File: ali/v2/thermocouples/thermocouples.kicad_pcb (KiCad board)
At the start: 4 copper layers, 85 x 76 mm, 169 parts, among them J1 Conn_02x01, J10 Conn_01x02, J11 Conn_01x02, J12 Conn_01x02, J13 Conn_01x02, J14 Conn_01x02, J15 Conn_01x15, J2 Conn_01x05, J3 USB_C_Receptacle_USB2.0_16P, J5 Conn_02x09_Counter_Clockwise, J6 Screw_Terminal_01x02, J7 Conn_01x03, J8 Vertical Ethernet, J9 Conn_01x02, SW1 SKRPANE010, U1 STM32H563RIV6, U10 TMP117AIDRVR, U11 TMP117AIDRVR, U12 TMP117AIDRVR, U13 TMP117AIDRVR, U2 UCC33420-Q1, U3 AP2112K-3.3, U4 TJA1462ATK, U5 LAN8742AI, U6 ADS124S08, U7 TCA9543A, U8 TMP117AIDRVR, U9 TMP117AIDRVR, Y1 25 MHz, Y2 25 MHz

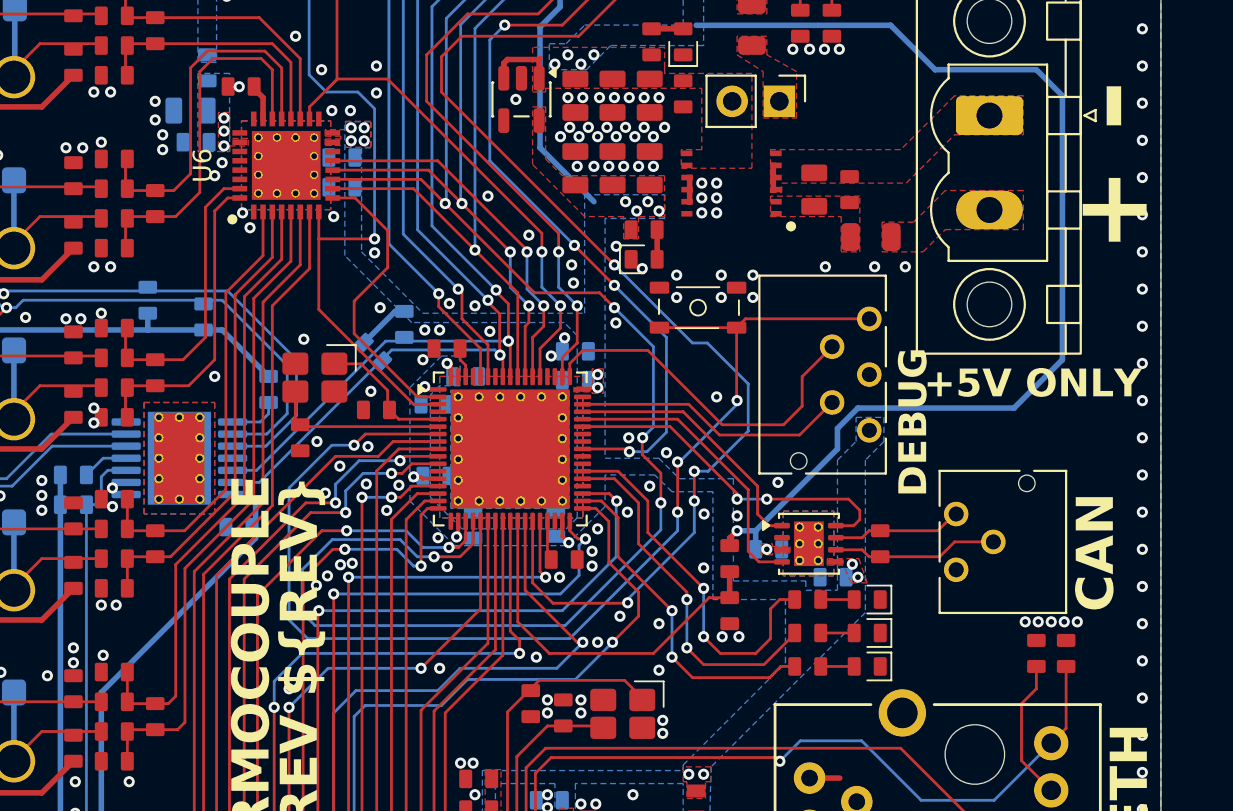
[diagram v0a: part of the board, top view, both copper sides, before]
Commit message: Globally remove LCSC labels, update MPNs and IOCs, add +5V monitoring to DAQs, fix some footprints
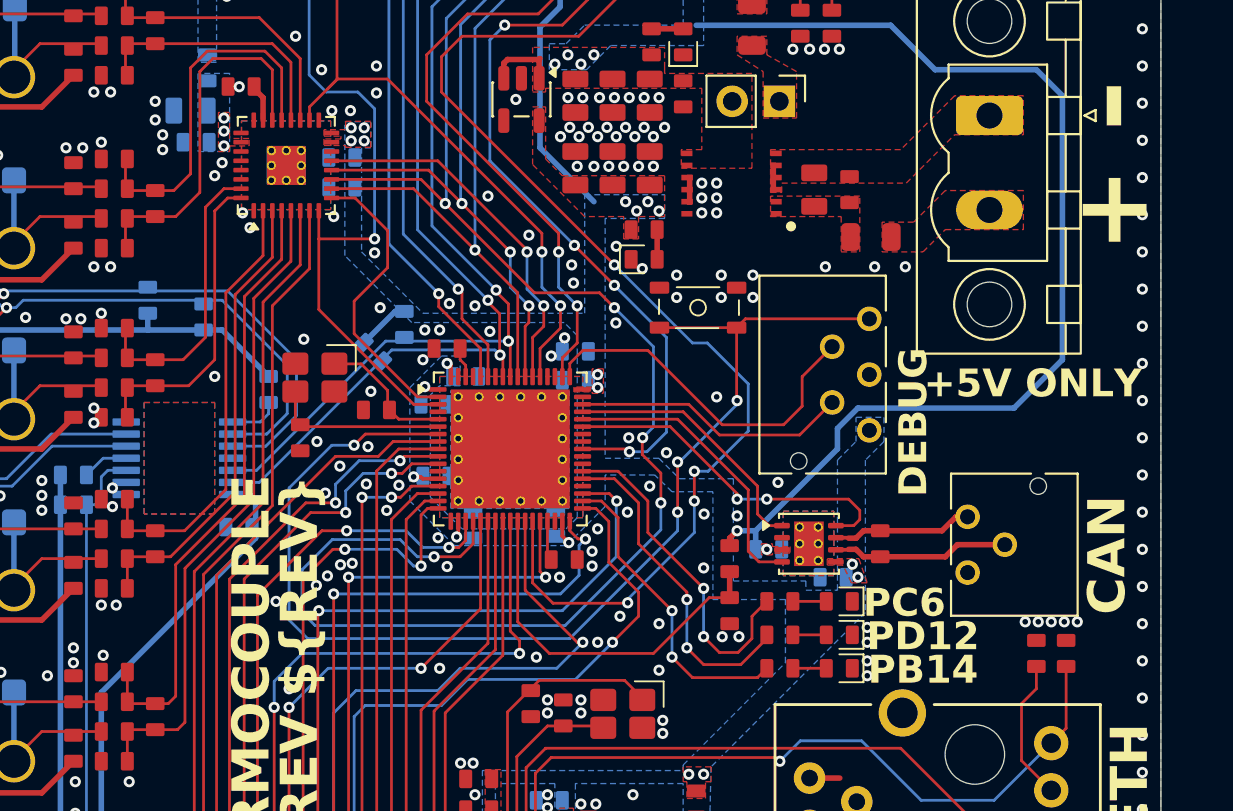
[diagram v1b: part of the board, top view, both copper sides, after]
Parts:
- U6: footprint APRL_Package:QFN-32_EP_5.8x5.8_Pitch0.5mm -> APRL_Package_QFN:Texas_RHB0032M_VQFN-32-1EP_5x5mm_P0.5mm_EP2.1x2.1mm_ThermalVias
- U7: footprint Package_SO:Texas_HTSSOP-14-1EP_4.4x5mm_P0.65mm_EP3.4x5mm_Mask3.155x3.255mm_ThermalVias -> APRL_Package:TSSOP-14_4.4x5mm_P0.65mm
- moved D1 1.50 mm to (163.4, 110.7)
- moved D4 1.50 mm to (163.4, 108.9)
- moved D5 1.50 mm to (163.4, 107.1)
- moved R5 1.50 mm to (160.2, 110.7)
- moved R6 1.50 mm to (160.2, 108.9)
- moved R7 1.50 mm to (160.2, 107.1)
- moved J7 0.63 mm to (170.3, 102.6)
- renumbered C50 to C32, C49 to C33, C36 to C34, C37 to C35, C38 to C36, C39 to C37, C52 to C38, C51 to C39, C54 to C40, C53 to C41, C43 to C42, C42 to C43, C45 to C44, C44 to C45, C48 to C46, C46 to C48, C33 to C49, C32 to C50, C35 to C51, C34 to C52, C41 to C53, C40 to C54, D12 to D10, D13 to D11, D10 to D12, D11 to D13, D8 to D14, D9 to D15, D6 to D16, D7 to D17, D4 to D2, D5 to D3, D2 to D4, D3 to D5, D16 to D6, D17 to D7, D14 to D8, D15 to D9, J15 to J4, R8 to R10, R9 to R11, R10 to R12, R11 to R13, R12 to R14, R13 to R15, R14 to R16, R15 to R17, R16 to R18, R17 to R19, R18 to R20, R37 to R21, R36 to R22, R39 to R24, R38 to R25, R41 to R26, R40 to R27, R43 to R28, R42 to R29, R4 to R3, R29 to R30, R28 to R31, R31 to R32, R30 to R33, R33 to R34, R32 to R35, R35 to R36, R34 to R37, R20 to R38, R19 to R39, R5 to R4, R22 to R40, R21 to R41, R25 to R42, R24 to R43, R27 to R44, R26 to R45, R44 to R46, R45 to R47, R46 to R48, R47 to R49, R3 to R5, R48 to R50, R49 to R51, R50 to R52, R51 to R53, R52 to R54, R53 to R8, R54 to R9
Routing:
- net /Microcontroller/USER_LED_3: track 20.1 -> 18.3 mm
- net /Microcontroller/USER_LED_2: track 19.3 -> 17.7 mm
- net /Microcontroller/USER_LED_1: track 18.3 -> 16.7 mm
- net Net-(J7-Pin_1): track 6.91 -> 7.57 mm
- net Net-(J7-Pin_2): track 8.96 -> 9.53 mm
- net GND: vias 349 -> 354
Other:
- board text added: "PB14"
- board text added: "PC6"
- board text added: "PD12"

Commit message: Small documentation
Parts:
- moved R49 11.5 mm to (122.2, 100.3), turned to 0 degrees
- moved R50 11.5 mm to (132.7, 95.7), turned to -90 degrees
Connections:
- R49 pad 2: Net-(U7-~{INT1}) -> Net-(U7-~{INT0})
- R50 pad 2: Net-(U7-~{INT0}) -> Net-(U7-~{INT1})

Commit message: Small TC changes, small just script fixes
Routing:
- net GND: track 1.62 -> 4.33 mm
